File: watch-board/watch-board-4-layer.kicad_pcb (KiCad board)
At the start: 4 copper layers, 34 x 34 mm, 64 parts, among them J1 Conn_PAD, J2 Conn_PAD, J3 Conn_PAD, J4 Conn_PAD, J5 Conn_PAD, Q1 Phototransistor_ALS-PT19-315C, Q2 Phototransistor_ALS-PT19-315C, Q3 Transistor_MMBT3904-TP, U1 Display-Driver_PCA8561ANH, U2 Regulator_BQ25504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

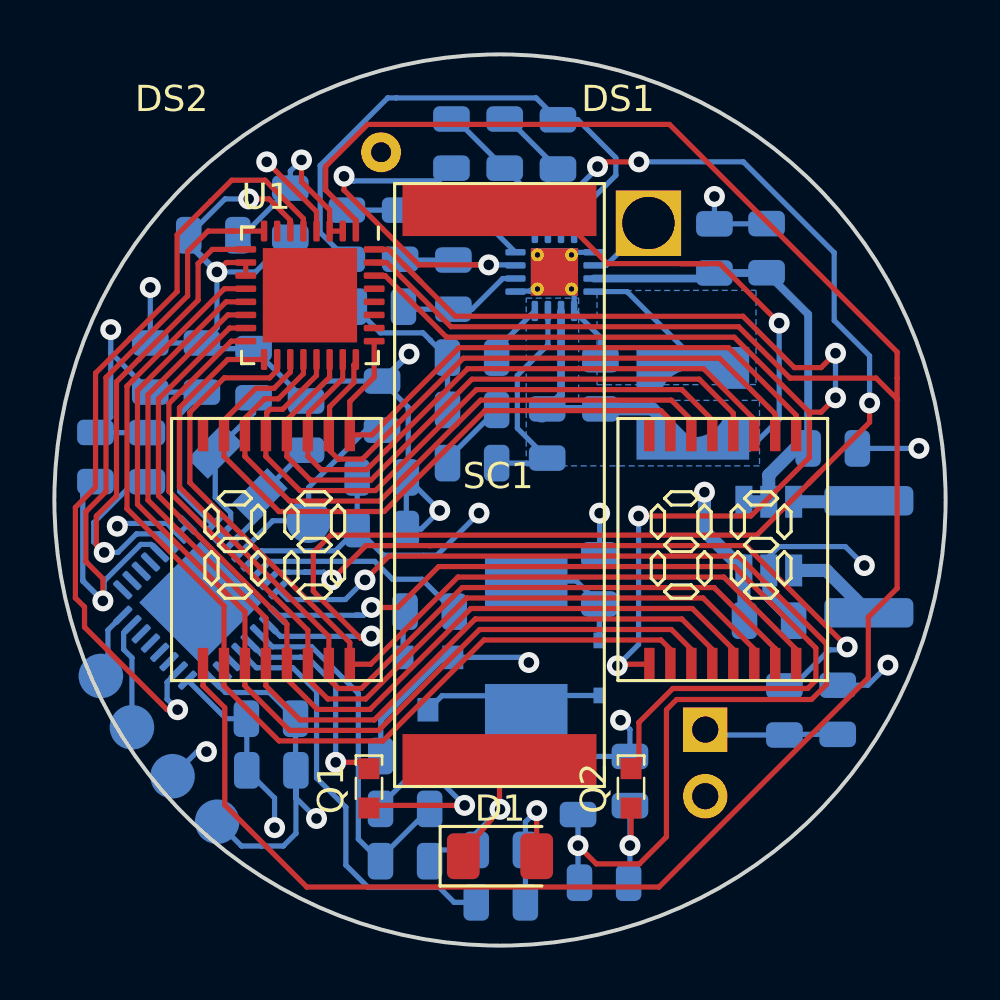
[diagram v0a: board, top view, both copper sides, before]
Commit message: four layer complete -- need to do silk screen
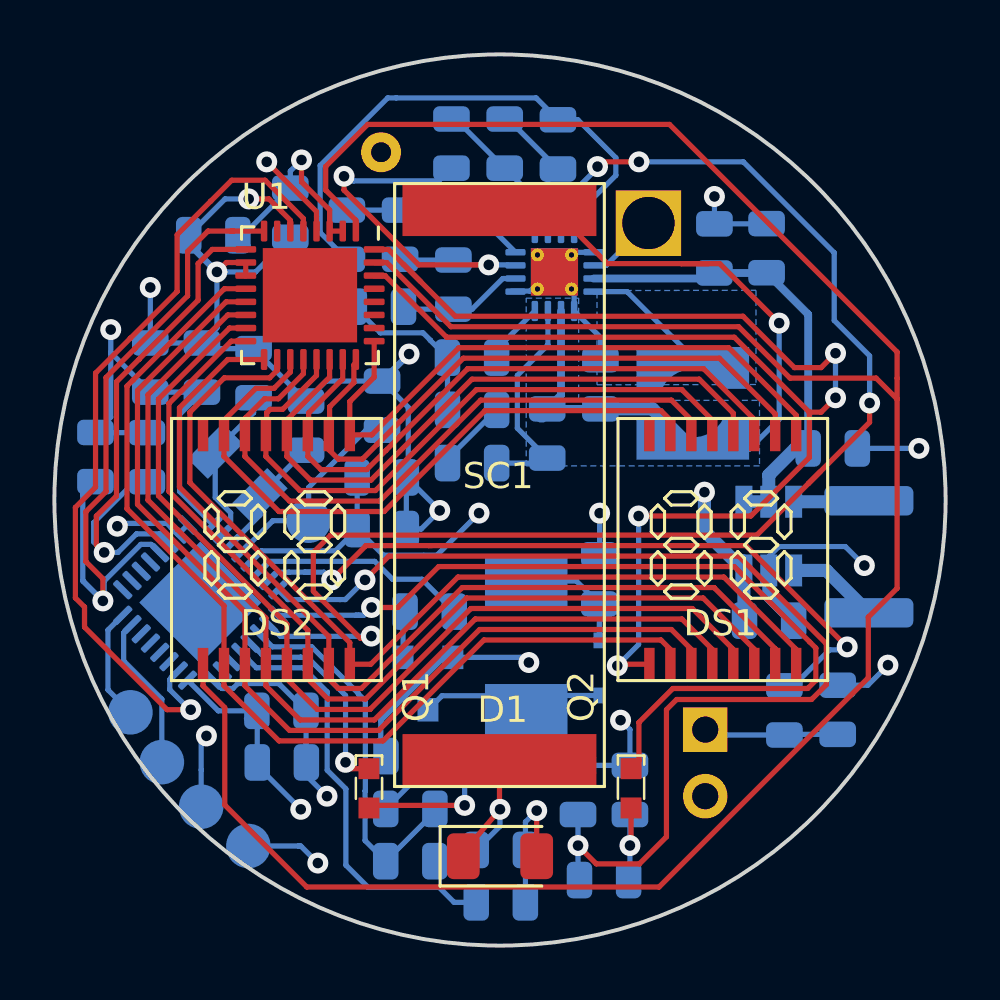
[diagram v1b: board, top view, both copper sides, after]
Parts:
- moved J2 1.79 mm to (125.9, 108.1)
- moved J3 1.75 mm to (127.1, 110.0)
- moved J5 1.59 mm to (128.6, 111.7)
- moved J4 1.51 mm to (130.4, 113.2)
- moved C8 0.50 mm to (131.7, 108.0)
- moved C9 0.50 mm to (131.7, 110.0)
- moved R19 0.34 mm to (145.0, 111.1)
- moved R16 0.20 mm to (136.6, 109.8)
- moved C18 0.20 mm to (136.6, 113.8)
- moved R17 0.20 mm to (136.6, 111.8)
- moved R21 0.10 mm to (144.0, 114.5)
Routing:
- net GND: track 130.9 -> 128.9 mm, vias 15 -> 16
- net /SWDIO: track 4.18 -> 6.06 mm
- net /SWCLK: track 2.65 -> 4.29 mm
- net VDD: track 55.0 -> 55.9 mm
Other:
- board text added: "CLK"
- board text added: "DIO"
- board text added: "GND"
- board text added: "RST"
- board text added: "VDD"
